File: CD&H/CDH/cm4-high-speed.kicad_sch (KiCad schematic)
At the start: 5 parts, among them J4 USB_OTG, U2 TPD2EUSB30

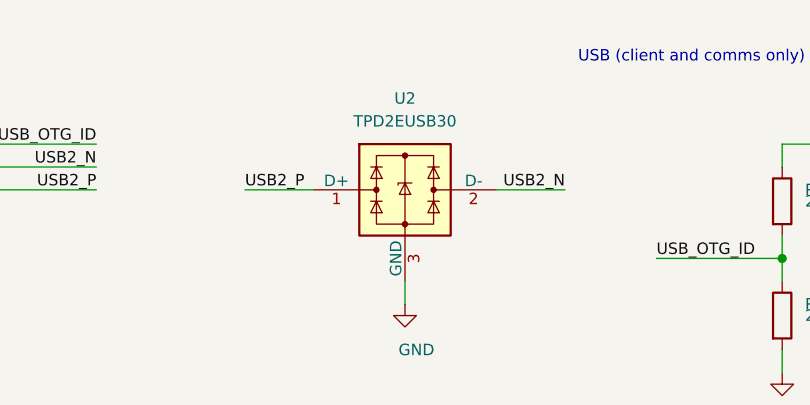
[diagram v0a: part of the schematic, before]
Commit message: modifications for v2
CDH: UART connector relocation, LED relocation, removed EEPROM solder jumper
Payload: Removed connection to GND of unconnected ground-plane pins, adjusted traces
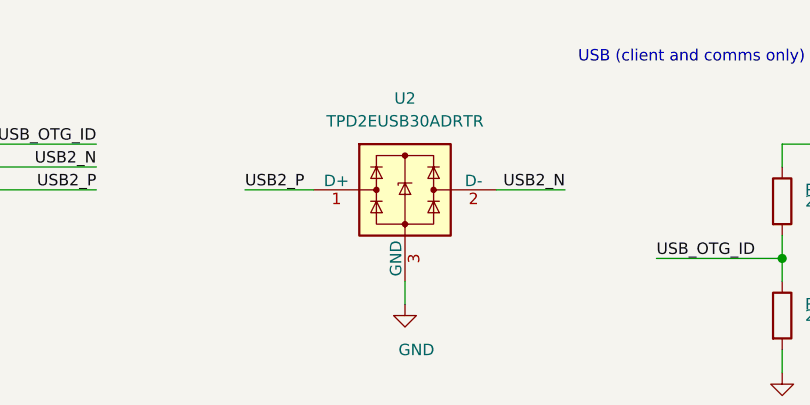
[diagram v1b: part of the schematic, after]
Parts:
- U2: value TPD2EUSB30 -> TPD2EUSB30ADRTR; MPN TPD2EUSB30DRTR -> TPD2EUSB30ADRTR
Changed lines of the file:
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@@
     (in_bom yes) (on_board yes)
     (property "Reference" "U2" (id 0) (at 153.67 40.64 0))
-    (property "Value" "TPD2EUSB30" (id 1) (at 153.67 43.18 0))
+    (property "Value" "TPD2EUSB30ADRTR" (id 1) (at 153.67 43.18 0))
     (property "Footprint" "Package_TO_SOT_SMD:Texas_DRT-3" (id 2) (at 134.62 58.42 0)
       (effects (font (size 1.27 1.27)) hide)
@@
       (effects (font (size 1.27 1.27)) hide)
     )
-    (property "MPN" "TPD2EUSB30DRTR" (id 5) (at 153.67 50.8 0)
+    (property "MPN" "TPD2EUSB30ADRTR" (id 5) (at 153.67 50.8 0)
       (effects (font (size 1.27 1.27)) hide)
     )
